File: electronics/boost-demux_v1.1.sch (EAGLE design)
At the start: 46 parts, among them M1 6-32_MOUNT, M2 6-32_MOUNT, M3 6-32_MOUNT, M4 6-32_MOUNT, Q1 ON_FDD4141, U1 TI_TPS55330, U2 4067D, U5 AVAGO_ACPL-217

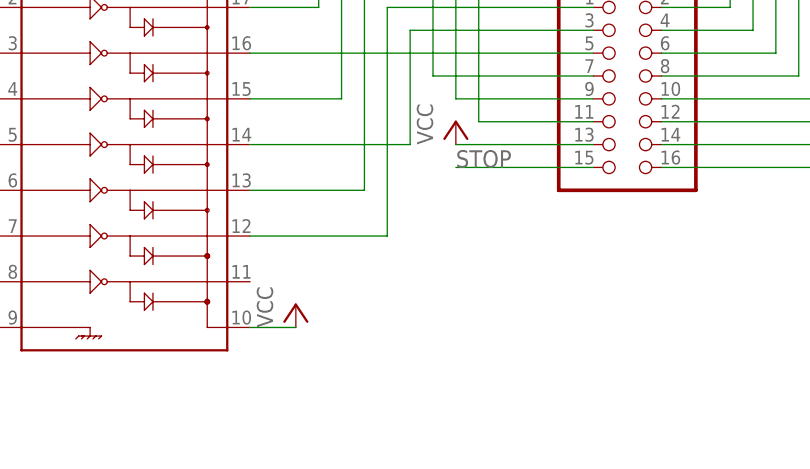
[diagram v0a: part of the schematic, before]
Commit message: Electronics v1.1 draft updates
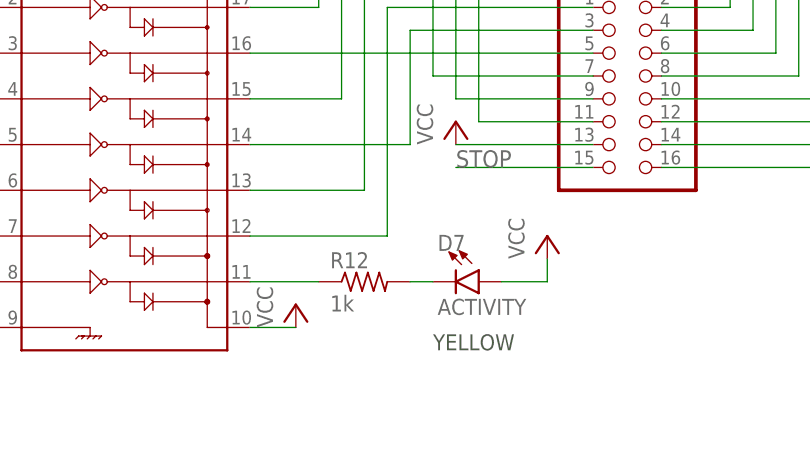
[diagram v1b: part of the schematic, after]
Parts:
- added D7: ACTIVITY, SparkFun-LED:LED5MM
- added R12: 1k, resistor:R-US_R1206
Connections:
- new net N$12: R12.1, U3.11
- new net N$42: D7.C, R12.2
- net VCC: now also D7.A
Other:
- note added: "YELLOW"
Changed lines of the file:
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@@
 <part name="M4" library="components" deviceset="6-32_MOUNT" device=""/>
 <part name="LOGO1" library="components" deviceset="MADOG" device=""/>
+<part name="D7" library="SparkFun-LED" deviceset="LED" device="5MM" value="ACTIVITY"/>
+<part name="P+7" library="supply1" library_urn="urn:adsk.eagle:library:371" deviceset="VCC" device=""/>
+<part name="R12" library="resistor" library_urn="urn:adsk.eagle:library:348" deviceset="R-US_" device="R1206" package3d_urn="urn:adsk.eagle:package:26062/1" value="1k"/>
 </parts>
 <sheets>
@@
 <text x="78.74" y="30.48" size="1.778" layer="97" rot="R90">GREEN</text>
 <text x="91.44" y="30.48" size="1.778" layer="97" rot="R90">RED</text>
+<text x="203.2" y="7.62" size="1.778" layer="97">YELLOW</text>
 </plain>
 <instances>
@@
 <instance part="M4" gate="G$1" x="220.98" y="111.76"/>
 <instance part="LOGO1" gate="G$1" x="12.7" y="43.18"/>
+<instance part="D7" gate="G$1" x="208.28" y="15.24" rot="R270"/>
+<instance part="P+7" gate="VCC" x="215.9" y="20.32"/>
+<instance part="R12" gate="G$1" x="195.58" y="15.24"/>
 </instances>
 <busses>
@@
 <wire x1="220.98" y1="30.48" x2="205.74" y2="30.48" width="0.1524" layer="91"/>
 </segment>
+<segment>
+<pinref part="P+7" gate="VCC" pin="VCC"/>
+<wire x1="215.9" y1="17.78" x2="215.9" y2="15.24" width="0.1524" layer="91"/>
+<pinref part="D7" gate="G$1" pin="A"/>
+<wire x1="215.9" y1="15.24" x2="210.82" y2="15.24" width="0.1524" layer="91"/>
+</segment>
 </net>
 <net name="N$6" class="0">
@@
 </segment>
 </net>
+<net name="N$12" class="0">
+<segment>
+<pinref part="U3" gate="G$1" pin="11"/>
+<pinref part="R12" gate="G$1" pin="1"/>
+<wire x1="182.88" y1="15.24" x2="190.5" y2="15.24" width="0.1524" layer="91"/>
+</segment>
+</net>
+<net name="N$42" class="0">
+<segment>
+<pinref part="R12" gate="G$1" pin="2"/>
+<pinref part="D7" gate="G$1" pin="C"/>
+<wire x1="200.66" y1="15.24" x2="203.2" y2="15.24" width="0.1524" layer="91"/>
+</segment>
+</net>

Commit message: PCBs v1.1 final
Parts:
- added TP1, TP2, TP3, TP4: TPB1,27, testpad:TPB1,27
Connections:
- net +12V: now also TP2.TP
- net +20V: now also TP3.TP
- net +5V: now also TP1.TP
- net GND: now also TP4.TP
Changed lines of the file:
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@@
 <layers>
 <layer number="1" name="Top" color="4" fill="1" visible="no" active="no"/>
+<layer number="2" name="Route2" color="1" fill="3" visible="no" active="no"/>
+<layer number="3" name="Route3" color="4" fill="3" visible="no" active="no"/>
+<layer number="4" name="Route4" color="1" fill="4" visible="no" active="no"/>
+<layer number="5" name="Route5" color="4" fill="4" visible="no" active="no"/>
+<layer number="6" name="Route6" color="1" fill="8" visible="no" active="no"/>
+<layer number="7" name="Route7" color="4" fill="8" visible="no" active="no"/>
+<layer number="8" name="Route8" color="1" fill="2" visible="no" active="no"/>
+<layer number="9" name="Route9" color="4" fill="2" visible="no" active="no"/>
+<layer number="10" name="Route10" color="1" fill="7" visible="no" active="no"/>
+<layer number="11" name="Route11" color="4" fill="7" visible="no" active="no"/>
+<layer number="12" name="Route12" color="1" fill="5" visible="no" active="no"/>
+<layer number="13" name="Route13" color="4" fill="5" visible="no" active="no"/>
+<layer number="14" name="Route14" color="1" fill="6" visible="no" active="no"/>
+<layer number="15" name="Route15" color="4" fill="6" visible="no" active="no"/>
 <layer number="16" name="Bottom" color="1" fill="1" visible="no" active="no"/>
 <layer number="17" name="Pads" color="2" fill="1" visible="no" active="no"/>
@@
 <part name="P+7" library="supply1" library_urn="urn:adsk.eagle:library:371" deviceset="VCC" device=""/>
 <part name="R12" library="resistor" library_urn="urn:adsk.eagle:library:348" deviceset="R-US_" device="R1206" package3d_urn="urn:adsk.eagle:package:26062/1" value="1k"/>
+<part name="TP1" library="testpad" library_urn="urn:adsk.eagle:library:385" deviceset="TP" device="B1,27" package3d_urn="urn:adsk.eagle:package:27944/1" value="TPB1,27"/>
+<part name="TP2" library="testpad" library_urn="urn:adsk.eagle:library:385" deviceset="TP" device="B1,27" package3d_urn="urn:adsk.eagle:package:27944/1" value="TPB1,27"/>
+<part name="TP3" library="testpad" library_urn="urn:adsk.eagle:library:385" deviceset="TP" device="B1,27" package3d_urn="urn:adsk.eagle:package:27944/1" value="TPB1,27"/>
+<part name="TP4" library="testpad" library_urn="urn:adsk.eagle:library:385" deviceset="TP" device="B1,27" package3d_urn="urn:adsk.eagle:package:27944/1" value="TPB1,27"/>
+<part name="GND5" library="supply1" library_urn="urn:adsk.eagle:library:371" deviceset="GND" device=""/>
 </parts>
 <sheets>
@@
 <instance part="P+7" gate="VCC" x="215.9" y="20.32"/>
 <instance part="R12" gate="G$1" x="195.58" y="15.24"/>
+<instance part="TP1" gate="G$1" x="58.42" y="45.72"/>
+<instance part="TP2" gate="G$1" x="68.58" y="45.72"/>
+<instance part="TP3" gate="G$1" x="78.74" y="45.72"/>
+<instance part="TP4" gate="G$1" x="101.6" y="45.72"/>
+<instance part="GND5" gate="1" x="101.6" y="35.56"/>
 </instances>
 <busses>
@@
 <pinref part="P+6" gate="1" pin="+12V"/>
 <pinref part="D3" gate="G$1" pin="A"/>
-<wire x1="73.66" y1="35.56" x2="73.66" y2="30.48" width="0.1524" layer="91"/>
+<wire x1="73.66" y1="35.56" x2="73.66" y2="33.02" width="0.1524" layer="91"/>
+<pinref part="TP2" gate="G$1" pin="TP"/>
+<wire x1="73.66" y1="33.02" x2="73.66" y2="30.48" width="0.1524" layer="91"/>
+<wire x1="73.66" y1="33.02" x2="68.58" y2="33.02" width="0.1524" layer="91"/>
+<wire x1="68.58" y1="33.02" x2="68.58" y2="43.18" width="0.1524" layer="91"/>
+<junction x="73.66" y="33.02"/>
 </segment>
 </net>
@@
 <junction x="50.8" y="81.28"/>
 </segment>
+<segment>
+<pinref part="TP4" gate="G$1" pin="TP"/>
+<pinref part="GND5" gate="1" pin="GND"/>
+<wire x1="101.6" y1="43.18" x2="101.6" y2="38.1" width="0.1524" layer="91"/>
+</segment>
 </net>
 <net name="N$1" class="0">
@@
 <pinref part="P+5" gate="1" pin="+5V"/>
 <pinref part="D2" gate="G$1" pin="A"/>
-<wire x1="63.5" y1="35.56" x2="63.5" y2="30.48" width="0.1524" layer="91"/>
+<wire x1="63.5" y1="35.56" x2="63.5" y2="33.02" width="0.1524" layer="91"/>
+<pinref part="TP1" gate="G$1" pin="TP"/>
+<wire x1="63.5" y1="33.02" x2="63.5" y2="30.48" width="0.1524" layer="91"/>
+<wire x1="63.5" y1="33.02" x2="58.42" y2="33.02" width="0.1524" layer="91"/>
+<wire x1="58.42" y1="33.02" x2="58.42" y2="43.18" width="0.1524" layer="91"/>
+<junction x="63.5" y="33.02"/>
 </segment>
 <segment>
@@
 <segment>
 <pinref part="D4" gate="G$1" pin="A"/>
-<wire x1="83.82" y1="38.1" x2="83.82" y2="30.48" width="0.1524" layer="91"/>
+<wire x1="83.82" y1="38.1" x2="83.82" y2="33.02" width="0.1524" layer="91"/>
 <label x="83.82" y="33.02" size="1.778" layer="95" rot="R90"/>
-</segment>
-</net>
+<pinref part="TP3" gate="G$1" pin="TP"/>
+<wire x1="83.82" y1="33.02" x2="83.82" y2="30.48" width="0.1524" layer="91"/>
+<wire x1="83.82" y1="33.02" x2="78.74" y2="33.02" width="0.1524" layer="91"/>
+<wire x1="78.74" y1="33.02" x2="78.74" y2="43.18" width="0.1524" layer="91"/>
+<junction x="83.82" y="33.02"/>
+</segment>
+</net>
